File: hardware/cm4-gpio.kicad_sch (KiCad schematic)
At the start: 6 parts, among them J2 DF40C-100DP-0.4V_51_

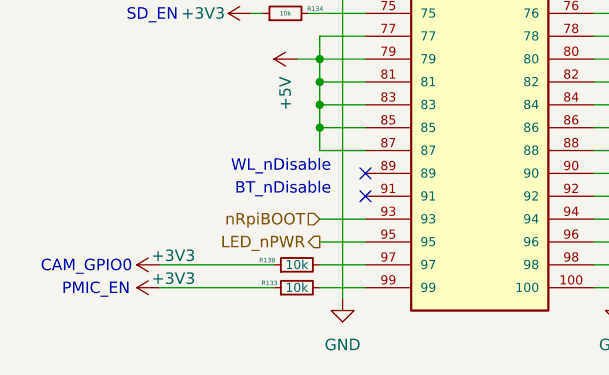
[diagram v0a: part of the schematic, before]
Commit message: fix #26 fix #24
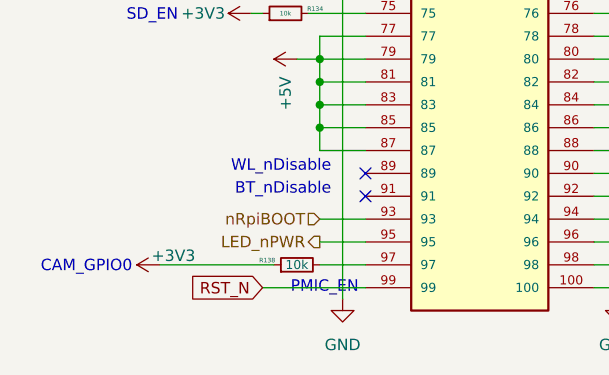
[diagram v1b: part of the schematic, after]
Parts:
- removed R133: 10k, Resistor_SMD:R_0402_1005Metric, symbol Device:R_Small
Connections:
- net RST_N: now also J2.99
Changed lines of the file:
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@@
 	(text "PMIC_EN"
 		(exclude_from_sim no)
-		(at 33.528 151.384 0)
+		(at 58.928 151.13 0)
 		(effects
 			(font
@@
 	(wire
 		(pts
-			(xy 54.61 151.13) (xy 59.69 151.13)
+			(xy 48.26 151.13) (xy 59.69 151.13)
 		)
 		(stroke
@@
 	(wire
 		(pts
-			(xy 36.83 151.13) (xy 49.53 151.13)
-		)
-		(stroke
-			(width 0)
-			(type default)
-		)
-	)
-	(wire
-		(pts
 			(xy 46.99 82.55) (xy 59.69 82.55)
 		)
@@
 		)
 	)
+	(global_label "RST_N"
+		(shape input)
+		(at 48.26 151.13 180)
+		(fields_autoplaced yes)
+		(effects
+			(font
+				(size 1.27 1.27)
+			)
+			(justify right)
+		)
+		(property "Intersheetrefs" "${INTERSHEET_REFS}"
+			(at 39.5296 151.13 0)
+			(effects
+				(font
+					(size 1.27 1.27)
+				)
+				(justify right)
+				(hide yes)
+			)
+		)
+	)
 	(global_label "PWR_BTN"
 		(shape input)
@@
 					(unit 1)
 				)
-			)
-		)
-	)
-	(symbol
-		(lib_id "power:+3V3")
-		(at 36.83 151.13 90)
-		(unit 1)
-		(exclude_from_sim no)
-		(in_bom yes)
-		(on_board yes)
-		(dnp no)
-		(property "Reference" "#PWR06"
-			(at 40.64 151.13 0)
-			(effects
-				(font
-					(size 1.27 1.27)
-				)
-				(hide yes)
-			)
-		)
-		(property "Value" "+3V3"
-			(at 38.354 150.114 90)
-			(effects
-				(font
-					(size 1.27 1.27)
-				)
-			)
-		)
-		(property "Footprint" ""
-			(at 36.83 151.13 0)
-			(effects
-				(font
-					(size 1.27 1.27)
-				)
-				(hide yes)
-			)
-		)
-		(property "Datasheet" ""
-			(at 36.83 151.13 0)
-			(effects
-				(font
-					(size 1.27 1.27)
-				)
-				(hide yes)
-			)
-		)
-		(property "Description" "Power symbol creates a global label with name \"+3V3\""
-			(at 36.83 151.13 0)
-			(effects
-				(font
-					(size 1.27 1.27)
-				)
-				(hide yes)
-			)
-		)
-		(pin "1"
-		)
-		(instances
-			(project "ulx5m-gs"
-				(path "/9e5cbfd6-8186-4817-919e-acd256336bc8/283ab020-ff93-4a42-acab-3f426f9046f9"
-					(reference "#PWR06")
-					(unit 1)
-				)
-			)
-		)
-	)
-	(symbol
-		(lib_id "Device:R_Small")
-		(at 52.07 151.13 90)
-		(unit 1)
-		(exclude_from_sim no)
-		(in_bom yes)
-		(on_board yes)
-		(dnp no)
-		(property "Reference" "R133"
-			(at 49.022 150.622 90)
-			(effects
-				(font
-					(size 0.5 0.5)
-				)
-			)
-		)
-		(property "Value" "10k"
-			(at 52.07 151.13 90)
-			(effects
-				(font
-					(size 1 1)
-				)
-			)
-		)
-		(property "Footprint" "Resistor_SMD:R_0402_1005Metric"
-			(at 52.07 151.13 0)
-			(effects
-				(font
-					(size 1.27 1.27)
-				)
-				(hide yes)
-			)
-		)
-		(property "Datasheet" "~"
-			(at 52.07 151.13 0)
-			(effects
-				(font
-					(size 1.27 1.27)
-				)
-				(hide yes)
-			)
-		)
-		(property "Description" "Resistor, small symbol"
-			(at 52.07 151.13 0)
-			(effects
-				(font
-					(size 1.27 1.27)
-				)
-				(hide yes)
-			)
-		)
-		(pin "1"
-		)
-		(pin "2"
-		)
-		(instances
-			(project "ulx5m-gs"
-				(path "/9e5cbfd6-8186-4817-919e-acd256336bc8/283ab020-ff93-4a42-acab-3f426f9046f9"
-					(reference "R133")
-					(unit 1)
-				)

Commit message: minor schematic revisions
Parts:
- added R61, R62: 5k1, Resistor_SMD:R_0402_1005Metric, symbol Device:R_Small
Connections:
- net GND: now also R61.1, R62.1
- net at J2.94: now also R61.2
- net at J2.96: now also R62.2
- net FAN_PWM: no longer names the net of J2.19
- net ID_SC: no longer names the net of J2.35
- net ID_SD: no longer names the net of J2.36
- no-connect marks 6 -> 8
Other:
- note added: "CAM_GPIO1"
- note added: "USB_CC1"
- note added: "USB_CC2"
- moved on the sheet: J2, R128, R134, R138, R139
